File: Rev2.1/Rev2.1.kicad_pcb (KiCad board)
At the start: 2 copper layers, 115 parts, among them J1 Termination, J10 Conn_01x08_Pin, J11 3.3V power breakout, J12 5V power breakout, J13 8P8C_LED, J14 GPIO2, J2 CAN2, J3 Termination, J4 CAN1, J5 SWD, J6 USB_OTG, J7 GPIO1, J8 LIN Pots, J9 AIN, P2 USB_C_Plug_USB2.0, SW3 SW_SPDT, SW5 SW_Push, T1 H1102NLT, U1 STM32F429ZITx, U10 USBLC6-2P6(ESD protection), U12 USBLC6-4SC6, U2 TJA1051T, U3 AMS1117-3.3, U4 TJA1051T, U6 USBLC6-2P6(ESD protection), U7 MCP2200T-I-SO, U8 LAN8742A, U9 STMPS2151STR(Current protecti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, Y1 12MHz, Y2 16MHz, Y3 25Mhz

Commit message: done about 2/3 of the routing for the board
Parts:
- moved R34 19.8 mm to (150.5, 117.3), turned to 0 degrees
- moved R32 18.9 mm to (150.5, 114.2), turned to 0 degrees
- moved R38 17.6 mm to (153.2, 106.5), turned to 0 degrees
- moved R31 17.6 mm to (150.5, 115.8), turned to 0 degrees
- moved R44 15.4 mm to (153.2, 108.0), turned to 0 degrees
- moved R26 13.9 mm to (149.2, 126.0)
- moved R43 12.5 mm to (153.2, 109.5), turned to 0 degrees
- moved C2 11.3 mm to (155.3, 96.2), turned to 90 degrees
- moved R27 9.69 mm to (149.2, 127.8)
- moved C32 9.03 mm to (171.0, 74.5)
- moved C26 8.88 mm to (171.0, 65.5)
- moved C1 7.86 mm to (129.2, 80.0), turned to -90 degrees
- moved R40 7.58 mm to (154.8, 102.5), turned to -90 degrees
- moved R35 6.91 mm to (166.2, 120.5)
- moved R39 4.39 mm to (150.8, 105.8), turned to -90 degrees
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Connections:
- R10 pad 2: A2 -> A4
- R12 pad 2: A4 -> A1
- R17 pad 1: A1 -> A2
- R18 pad 1: A2 -> A4
- R19 pad 1: A4 -> A1
- R9 pad 2: A1 -> A2
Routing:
- net GND: track 0.00 -> 228.6 mm, vias 0 -> 70
- net ETH_MDC: track 0.00 -> 160.9 mm, vias 0 -> 4
- net +3.3V: track 0.00 -> 107.4 mm, vias 0 -> 19
- net REGOFF_LED: track 0.00 -> 54.7 mm, vias 0 -> 3
- net INTSEL_LED: track 0.00 -> 52.3 mm, vias 0 -> 3
- net /Ethernet/RX-: track 0.00 -> 46.8 mm
- net A1: track 0.00 -> 40.1 mm
- net Net-(J13-Pad4): track 0.00 -> 39.6 mm
- net /Ethernet/RX+: track 0.00 -> 36.3 mm
- net GP5: track 0.00 -> 36.0 mm, vias 0 -> 2
- net A3: track 0.00 -> 34.8 mm
- net GP4: track 0.00 -> 34.6 mm, vias 0 -> 2
- net A2: track 0.00 -> 33.4 mm
- net A4: track 0.00 -> 31.0 mm
- net GPIO8: track 0.00 -> 30.3 mm
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- added copper zone on In2.Cu, net +3.3V
- added copper zone on In1.Cu, net GND
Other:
- board outline added: 91.9 x 97.1 mm
- copper layers 2 -> 4

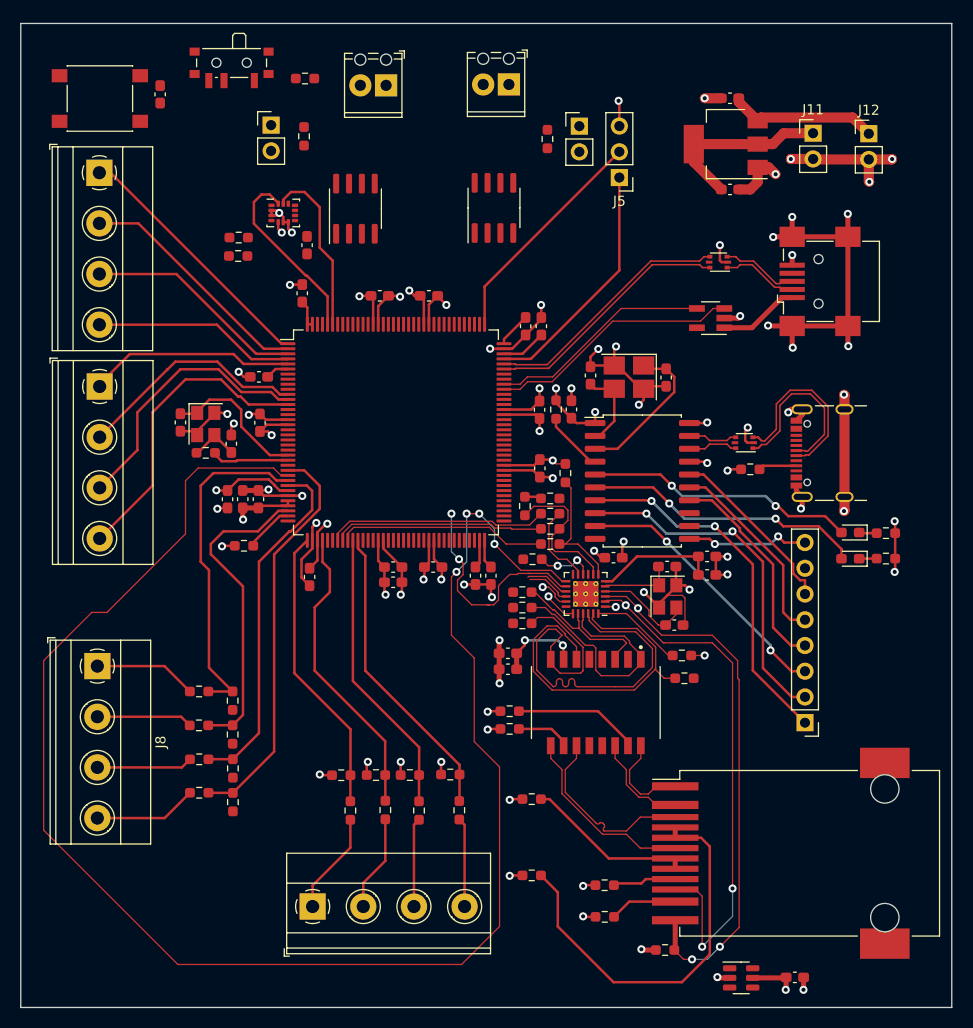
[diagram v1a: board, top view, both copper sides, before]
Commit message: finished the first mock up of routing now just need to polish it up
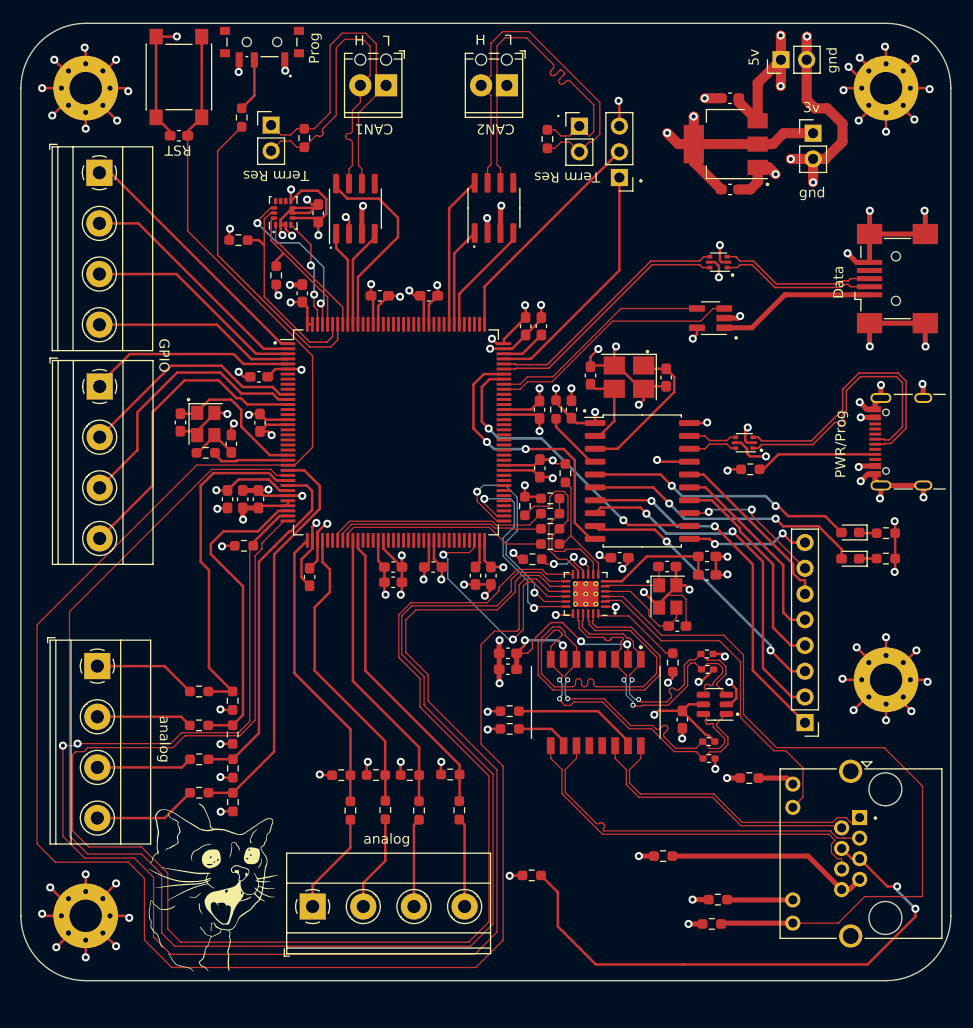
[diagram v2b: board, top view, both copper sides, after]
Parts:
- added G***: LOGO, LOGO, F.Cu at (119.8, 143.6)
- added G***: LOGO, LOGO, B.Cu at (143.6, 103.2)
- added H1: MountingHole_Pad, MountingHole:MountingHole_3.2mm_M3_Pad_Via, F.Cu at (107.4, 64.5)
- added H2: MountingHole_Pad, MountingHole:MountingHole_3.2mm_M3_Pad_Via, F.Cu at (107.4, 146.2)
- added H3: MountingHole_Pad, MountingHole:MountingHole_3.2mm_M3_Pad_Via, F.Cu at (186.4, 122.9)
- added H4: MountingHole_Pad, MountingHole:MountingHole_3.2mm_M3_Pad_Via, F.Cu at (186.4, 64.5)
- J13: footprint Connector_RJ:RJ45_Wuerth_74980111211_Horizontal -> Connector_RJ:RJ45_Amphenol_RJHSE538X
- R31, R32, R33, R34: footprint Resistor_SMD:R_0603_1608Metric_Pad0.98x0.95mm_HandSolder -> Resistor_SMD:R_0402_1005Metric_Pad0.72x0.64mm_HandSolder
- moved C5 27.8 mm to (166.3, 126.8), turned to -90 degrees
- moved U12 27.1 mm to (169.5, 125.3), turned to 180 degrees
- moved R34 22.8 mm to (168.9, 130.7), turned to 180 degrees
- moved R32 19.8 mm to (168.8, 121.9), turned to 180 degrees
- moved R31 18.8 mm to (168.7, 120.3), turned to 180 degrees
- moved R29 17.8 mm to (172.9, 132.6)
- moved R28 14.1 mm to (164.4, 140.3)
- moved J12 11.3 mm to (176.0, 61.7), turned to 90 degrees
- moved R30 11.3 mm to (169.8, 144.6)
- moved SW5 8.08 mm to (116.6, 63.4), turned to 90 degrees
- moved P2 7.86 mm to (189.0, 99.4)
- moved J6 7.64 mm to (187.4, 83.3)
- moved R3 7.34 mm to (122.8, 67.4), turned to 90 degrees
- moved R33 6.69 mm to (168.9, 129.0)
- moved J13 6.07 mm to (183.8, 136.5), turned to -90 degrees
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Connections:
- J6 pad 2: USB->ESD- -> USBData->ESD-
- J6 pad 3: USB->ESD+ -> USBData->ESD+
- P2 pad A6: USB->ESD+ -> /USB wiring/USB->ESD+
- P2 pad A7: USB->ESD- -> /USB wiring/USB->ESD-
- R43 pad 1: ETH_RXD1 -> Net-(U8-RXD1/MODE1)
- R43 pad 2: Net-(U8-RXD1/MODE1) -> ETH_RXD1
- U1 pad 110: Net-(U1-PA15) -> unconnected-(U1-PA15-Pad110)
- U1 pad 116: unconnected-(U1-PD2-Pad116) -> Silent_Mode1
- U1 pad 134: unconnected-(U1-PB4-Pad134) -> Silent_Mode2
- U1 pad 77: Net-(U1-PD8) -> unconnected-(U1-PD8-Pad77)
- U10 pad 1: USB->ESD- -> USBData->ESD-
- U10 pad 3: USB->ESD+ -> USBData->ESD+
- U2 pad 8: Net-(U1-PD8) -> Silent_Mode2
- U4 pad 8: Net-(U1-PA15) -> Silent_Mode1
- U6 pad 1: USB->ESD- -> /USB wiring/USB->ESD-
- U6 pad 3: USB->ESD+ -> /USB wiring/USB->ESD+
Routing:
- net NRST: track 4.42 -> 202.3 mm
- net ETH_MDIO: track 0.00 -> 151.4 mm
- net ETH_REF_CLK: track 27.6 -> 155.9 mm
- net GND: track 228.6 -> 323.1 mm, vias 70 -> 113
- net +3.3V: track 107.4 -> 147.1 mm, vias 19 -> 36
- net /CAN1+: track 0.00 -> 38.5 mm
- net /CAN1-: track 0.00 -> 38.5 mm
- net /CAN2-: track 0.00 -> 34.7 mm
- net /CAN2+: track 0.00 -> 34.6 mm
- net BOOT0: track 0.00 -> 31.1 mm
- net USART1_TX: track 0.00 -> 30.7 mm, vias 0 -> 2
- net USART1_RX: track 0.00 -> 27.9 mm, vias 0 -> 2
- net /USB wiring/USB->ESD+: track 0.00 -> 27.9 mm
- net /USB wiring/USB->ESD-: track 0.00 -> 27.9 mm
- net /Ethernet/RX+: track 36.3 -> 62.6 mm, vias 0 -> 2
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- added copper zone on In2.Cu, net +5V
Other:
- board size 91.9 x 97.1 mm -> 91.8 x 94.5 mm
- board text added: "3v"
- board text added: "5v"
- board text added: "CAN1"
- board text added: "CAN2"
- board text added: "Data"
- board text added: "GPIO"
- board text added: "H"
- board text added: "L"
- board text added: "PWR/Prog"
- board text added: "Prog"
- board text added: "RST"
- board text added: "Rev 2.1 4/13/24"
- board text added: "Term Res"
- board text added: "analog"
- board text added: "gnd"

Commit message: added user zone fills to section out the PCB into different sections
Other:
- board text added: "Analog Section"
- board text added: "CAN"
- board text added: "Digital Section"
- board text added: "Ethernet"
- board text added: "Power"
- board text added: "USB"
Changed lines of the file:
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@@
+    (effects (font (size 1 1) (thickness 0.15)) (justify left bottom))
+  )
+  (gr_text "Analog Section\n" (at 99.35 134.525 90) (layer "User.2")
+    (effects (font (size 1 1) (thickness 0.15)) (justify left bottom))
+  )
+  (gr_text "Digital Section\n" (at 99.875 94.275 90) (layer "User.4")
+    (effects (font (size 1 1) (thickness 0.15)) (justify left bottom))
+  )
+  (gr_text "Ethernet" (at 194.025 128.4 -90) (layer "User.5")
+    (effects (font (size 1 1) (thickness 0.15)) (justify left bottom))
+  )
+  (gr_text "USB" (at 193.825 89.75 -90) (layer "User.6")
+    (effects (font (size 1 1) (thickness 0.15)) (justify left bottom))
+  )
+  (gr_text "CAN" (at 141.325 57.475) (layer "User.7")
+    (effects (font (size 1 1) (thickness 0.15)) (justify left bottom))
+  )
+  (gr_text "Power" (at 176.625 57.35) (layer "User.8")
     (effects (font (size 1 1) (thickness 0.15)) (justify left bottom))
   )
@@
       )
     )
+  )
+  (zone (net 0) (net_name "") (layer "User.2") (hatch edge 0.5)
+    (connect_pads (clearance 0.5))
+    (min_thickness 0.25) (filled_areas_thickness no)
+    (fill yes (thermal_gap 0.5) (thermal_bridge_width 0.5))
+    (polygon
+      (pts
+        (xy 100.45 115.075)
+        (xy 147.575 115.05)
+        (xy 147.35 154.175)
+        (xy 99.975 154.4)
+        (xy 99.725 115.075)
+        (xy 100.525 115.075)
+      )
+    )
+  )
+  (zone (net 0) (net_name "") (layer "User.4") (hatch edge 0.5)
+    (connect_pads (clearance 0.5))
+    (min_thickness 0.25) (filled_areas_thickness no)
+    (fill yes (thermal_gap 0.5) (thermal_bridge_width 0.5))
+    (polygon
+      (pts
+        (xy 99.85 113.025)
+        (xy 115.85 112.775)
+        (xy 115.8 53.225)
+        (xy 95.85 53.225)
+        (xy 96.025 113.025)
+        (xy 99.925 113.025)
+      )
+    )
+  )
+  (zone (net 0) (net_name "") (layer "User.5") (hatch edge 0.5)
+    (connect_pads (clearance 0.5))
+    (min_thickness 0.25) (filled_areas_thickness no)
+    (fill yes (thermal_gap 0.5) (thermal_bridge_width 0.5))
+    (polygon
+      (pts
+        (xy 153.625 110.725)
+        (xy 201.575 110.675)
+        (xy 201.55 158.9)
+        (xy 151.85 158.675)
+        (xy 152.275 110.725)
+      )
+    )
+  )
+  (zone (net 0) (net_name "") (layer "User.6") (hatch edge 0.5)
+    (connect_pads (clearance 0.5))
+    (min_thickness 0.25) (filled_areas_thickness no)
+    (fill yes (thermal_gap 0.5) (thermal_bridge_width 0.5))
+    (polygon
+      (pts
+        (xy 195.25 110.325)
+        (xy 155.525 110.3)
+        (xy 155.475 76.425)
+        (xy 195.775 76.325)
+        (xy 195.95 110.325)
+      )
+    )
+  )
+  (zone (net 0) (net_name "") (layer "User.7") (hatch edge 0.5)
+    (connect_pads (clearance 0.5))
+    (min_thickness 0.25) (filled_areas_thickness no)
+    (fill yes (thermal_gap 0.5) (thermal_bridge_width 0.5))
+    (polygon
+      (pts
+        (xy 131.85 56.1)
+        (xy 131.9 65)
+        (xy 122.5 65)
+        (xy 122.525 74.125)
+        (xy 130.875 74.125)
+        (xy 130.875 81.1)
+        (xy 154.525 81.075)
+        (xy 154.525 75.325)
+        (xy 158.15 75.325)
+        (xy 158.1 56.15)
+        (xy 131.925 56.1)
+      )
+    )
+  )
+  (zone (net 0) (net_name "") (layer "User.8") (hatch edge 0.5)
+    (connect_pads (clearance 0.5))
+    (min_thickness 0.25) (filled_areas_thickness no)
+    (fill yes (thermal_gap 0.5) (thermal_bridge_width 0.5))
+    (polygon
+      (pts
+        (xy 163.25 55.975)
+        (xy 163.325 75.775)
+        (xy 195.525 75.775)
+        (xy 195.5 56)
+        (xy 163.425 55.975)
+      )
+    )

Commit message: added USART6 to some pin headers and added more labels and color codes to th schematic
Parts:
- added J15: USART6, Connector_PinHeader_2.54mm:PinHeader_1x03_P2.54mm_Vertical, F.Cu at (177.9, 89.3)
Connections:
- U1 pad 96: unconnected-(U1-PC6-Pad96) -> USART6_TX
- U1 pad 97: unconnected-(U1-PC7-Pad97) -> USART6_RX
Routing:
- net USART6_TX: track 0.00 -> 33.4 mm
- net USART6_RX: track 0.00 -> 33.1 mm
- net GND: track 323.1 -> 326.7 mm, vias 113 -> 115
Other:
- board text added: "CLK"
- board text added: "DIO"
- board text added: "GND"
- board text added: "RX"
- board text added: "TX"
- board text added: "UART6"
